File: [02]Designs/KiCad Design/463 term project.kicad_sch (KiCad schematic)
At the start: 143 parts, among them J1 Conn_01x02_Pin, J10 Conn_01x01_Pin, J11 Conn_01x01_Pin, J12 Conn_01x01_Pin, J13 Conn_01x01_Pin, J14 Conn_01x01_Pin, J15 Conn_01x01_Pin, J16 Conn_01x01_Pin, J17 Conn_01x01_Pin, J18 Conn_01x02_Pin, J19 Conn_01x02_Pin, J2 Screw_Terminal_01x01, J20 Conn_01x02_Pin, J21 Conn_01x02_Pin, J22 Conn_01x02_Pin, J23 Conn_01x02_Pin, J24 Conn_01x02_Pin, J25 Conn_01x02_Pin, J26 Conn_01x02_Pin, J3 Screw_Terminal_01x01, J4 Speed Measurement Sensor Conn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, J5 Screw_Terminal_01x01, J6 Screw_Terminal_01x01, J7 Conn_01x02_Pin, J8 Conn_01x01_Pin, J9 Conn_01x01_Pin, Q1 BC547, Q10 PJMH099N60EC, Q11 PJMH099N60EC, Q2 BC547, Q7 PJMH099N60EC, Q8 PJMH099N60EC, Q9 PJMH099N60EC, SW1 SW_Nidec_CAS-120A1, T2 Transformer, U1 6N135, U10 ADuM1200AR, U11 IR2110, U12 LM7805_TO220, U14 LM7815_TO220, U16 LD1117S33TR_SOT223, U17 LD1117S33TR_SOT223, U18 5 Button Module, U19 LM7812_TO220, U2 6N135, U20 LM7812_TO220, U3 74HC00, U4 IR2110, U5 IR2110, U6 ACS712xLCTR-30A, U8 ADuM1200AR, U9 ADuM1200AR

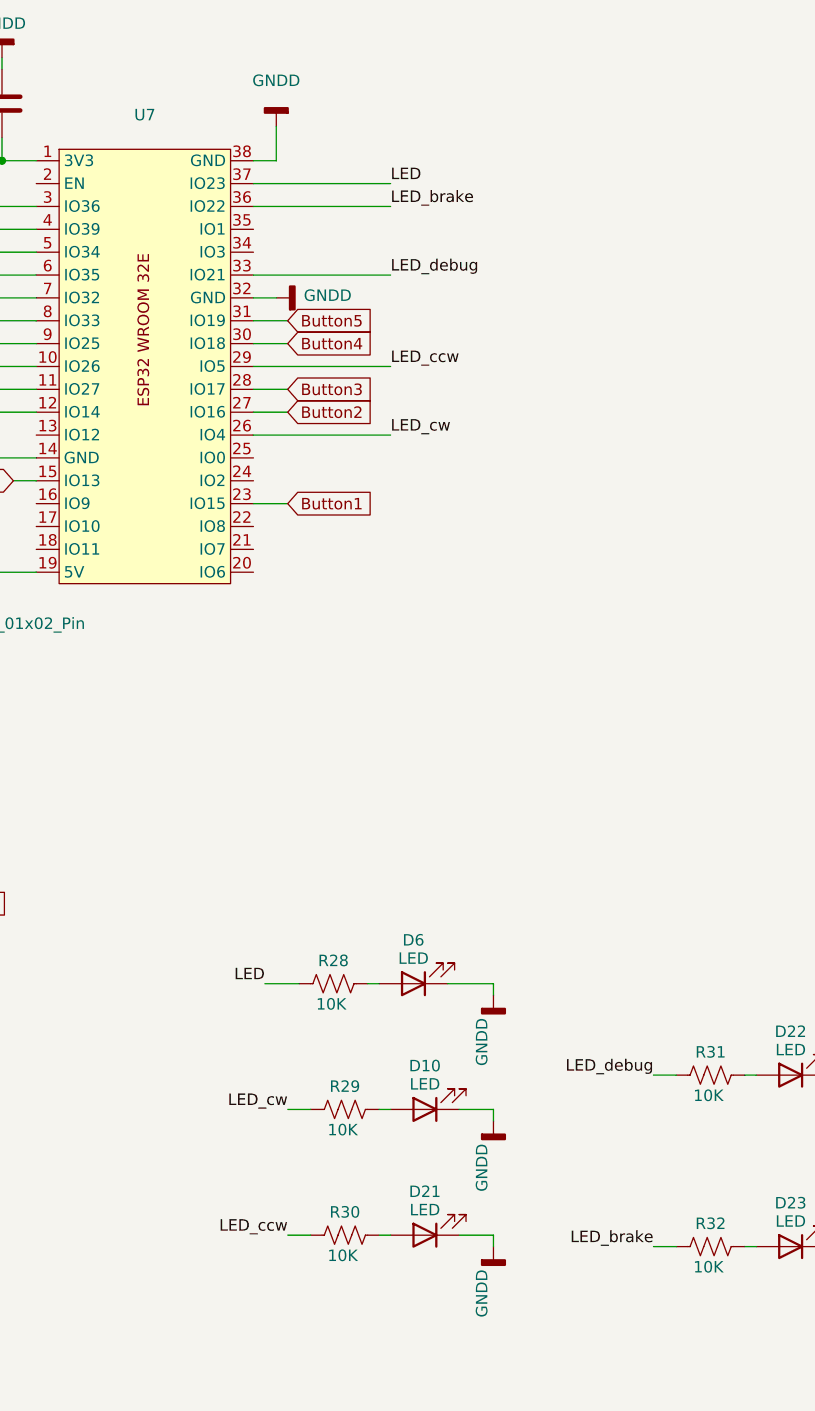
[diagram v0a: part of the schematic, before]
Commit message: Schematic Update & New Software Update (LED and Buttons Added)
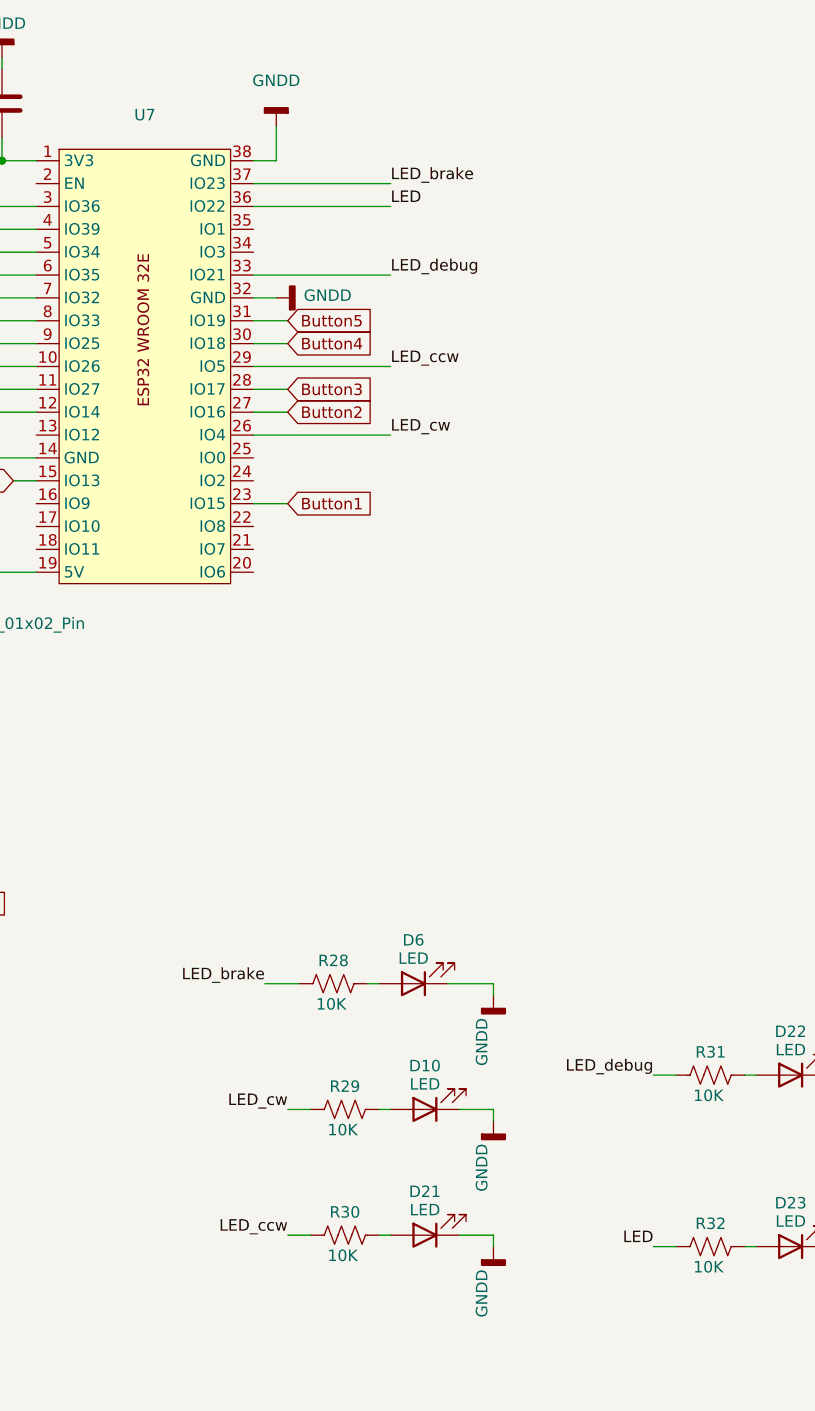
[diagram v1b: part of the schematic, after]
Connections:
- net LED: now also R32.1, U7.36 (IO22); no longer R28.1, U7.37 (IO23)
- net LED_brake: now also R28.1, U7.37 (IO23); no longer R32.1, U7.36 (IO22)
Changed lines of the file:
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@@
 	)
 	(label "LED_brake"
-		(at 377.19 363.22 180)
+		(at 334.01 334.01 180)
 		(effects
 			(font
@@
 			)
 			(justify right bottom)
-		)
-	)
-	(label "LED"
-		(at 347.98 245.11 0)
-		(effects
-			(font
-				(size 1.27 1.27)
-			)
-			(justify left bottom)
-		)
-	)
-	(label "LED_brake"
-		(at 347.98 247.65 0)
-		(effects
-			(font
-				(size 1.27 1.27)
-			)
-			(justify left bottom)
 		)
 	)
@@
 	(label "LED_cw"
 		(at 347.98 273.05 0)
+		(effects
+			(font
+				(size 1.27 1.27)
+			)
+			(justify left bottom)
+		)
+	)
+	(label "LED"
+		(at 347.98 247.65 0)
 		(effects
 			(font
@@
 		)
 	)
+	(label "LED_brake"
+		(at 347.98 245.11 0)
+		(effects
+			(font
+				(size 1.27 1.27)
+			)
+			(justify left bottom)
+		)
+	)
 	(label "LED_debug"
 		(at 347.98 255.27 0)
@@
 			)
 			(justify left bottom)
+		)
+	)
+	(label "LED"
+		(at 377.19 363.22 180)
+		(effects
+			(font
+				(size 1.27 1.27)
+			)
+			(justify right bottom)
 		)
 	)
@@
 		(effects
 			(font
-				(size 1.27 1.27)
-			)
-			(justify right bottom)
-		)
-	)
-	(label "LED"
-		(at 334.01 334.01 180)
-		(effects
-			(font
